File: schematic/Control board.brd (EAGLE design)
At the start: 37.1 x 55.9 mm, 14 parts, among them IC2 ATTINY44A

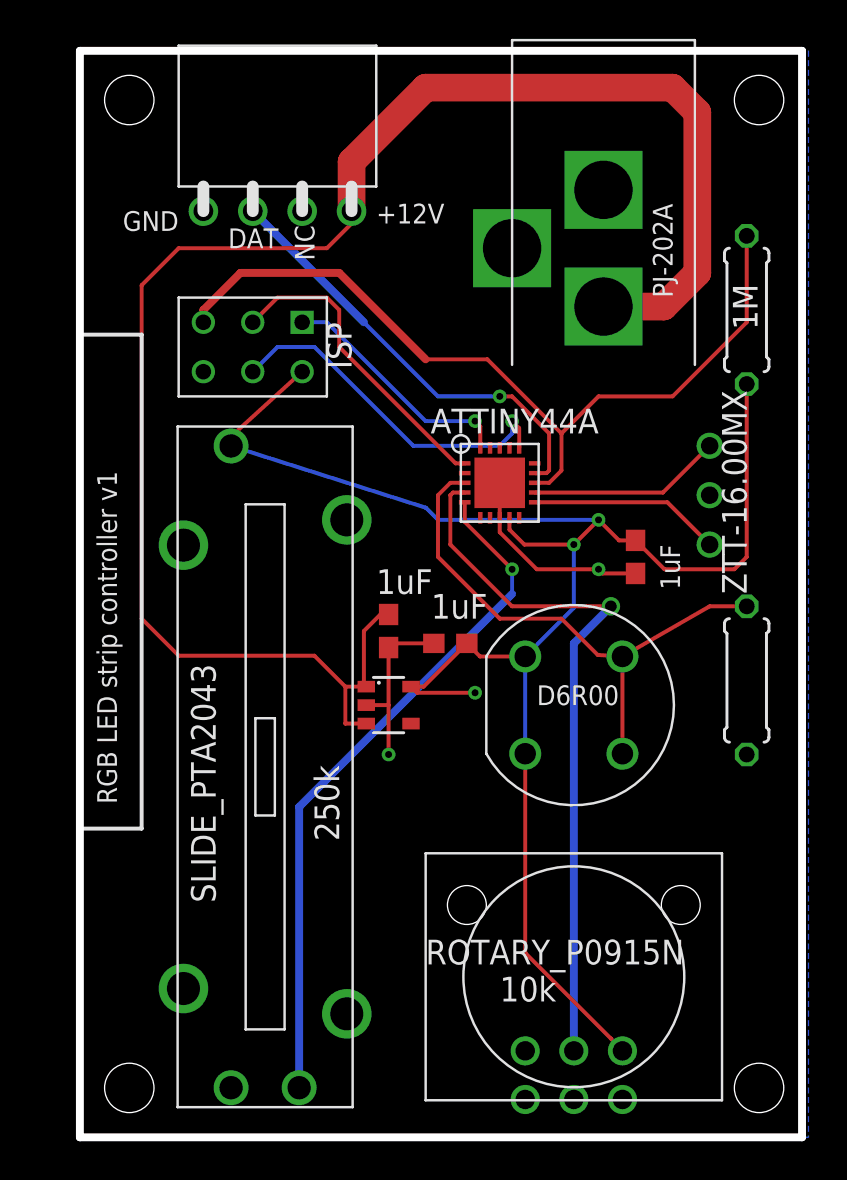
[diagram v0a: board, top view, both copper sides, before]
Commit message: Fixed value layers and line widths
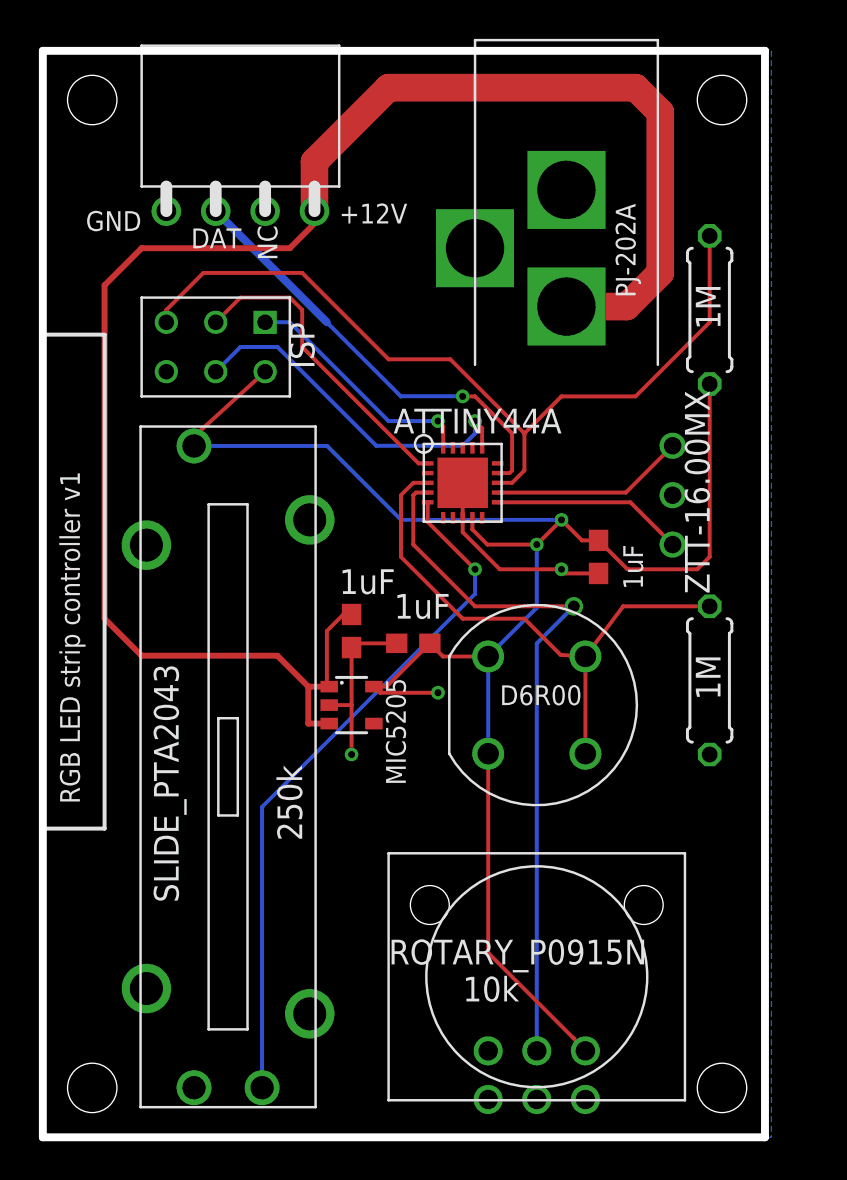
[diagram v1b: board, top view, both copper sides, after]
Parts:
- moved C1 1.91 mm to (15.9, 26.0)
- moved C3 1.91 mm to (28.6, 29.8)
- moved IC2 1.91 mm to (21.6, 33.7)
- moved R1 1.91 mm to (34.3, 23.5)
- moved R3 1.91 mm to (34.3, 42.5)
- moved REG1 1.91 mm to (15.9, 22.2)
- moved RES1 1.91 mm to (32.4, 33.0)
- moved ROTARY_P0915N 1.91 mm to (25.4, 4.45)
- moved S1 1.91 mm to (25.4, 22.2)
- moved CONN1 1.90 mm to (10.2, 47.6)
- moved SLIDE_PTA2043 1.90 mm to (9.53, 19.1)
- moved U$1 1.90 mm to (8.89, 40.6)
- moved C2 1.90 mm to (19.1, 25.4)
- moved POW1 1.90 mm to (22.2, 45.7)
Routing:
- net +5V: track 88.6 -> 89.4 mm
- net +12V: track 86.0 -> 86.6 mm
- net COLOR_SW: track 28.5 -> 29.1 mm

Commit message: Changed the resonator value from 16Mhz to 10MHz, for more accurate LED timing
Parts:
- RES1: value ZTT-16.00MX -> ZTT-10.00MT
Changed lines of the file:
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@@
 <attribute name="VALUE" x="34.8488" y="41.529" size="1.27" layer="21" font="vector" ratio="10" rot="R90"/>
 </element>
-<element name="RES1" library="RGB LED project" package="3-PIN-THROUGH-HOLE" value="ZTT-16.00MX" x="32.385" y="33.02" smashed="yes" rot="R90">
+<element name="RES1" library="RGB LED project" package="3-PIN-THROUGH-HOLE" value="ZTT-10.00MT" x="32.385" y="33.02" smashed="yes" rot="R90">
 <attribute name="VALUE" x="34.29" y="27.94" size="1.27" layer="21" font="vector" rot="R90"/>
 </element>

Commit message: Fixed the bounding area of the potentiometer, and adjusted the value of the reset line's pull-up resistor
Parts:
- R3: value 1M -> 10k
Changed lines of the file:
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@@
 <attribute name="VALUE" x="34.8488" y="22.479" size="1.27" layer="21" font="vector" ratio="10" rot="R90"/>
 </element>
-<element name="R3" library="resistor" package="0207/7" value="1M" x="34.29" y="42.545" smashed="yes" rot="R90">
+<element name="R3" library="resistor" package="0207/7" value="10k" x="34.29" y="42.545" smashed="yes" rot="R90">
 <attribute name="VALUE" x="34.8488" y="41.529" size="1.27" layer="21" font="vector" ratio="10" rot="R90"/>
 </element>
